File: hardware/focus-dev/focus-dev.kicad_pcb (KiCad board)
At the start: 2 copper layers, 100 x 90 mm, 133 parts, among them J1 USB_C_Receptacle_USB2.0_14P, J2 Conn_01x09, J3 IDC-10, J4 Conn_01x03, J5 Conn_01x01, J6 Conn_01x01, J7 Conn_01x01, J8 IDC-16, J9 XT60, Q1 IPD90N04S4L04, Q2 IPD90N04S4L04, Q3 IPD90N04S4L04, Q4 IPD90N04S4L04, Q5 IPD90N04S4L04, Q6 IPD90N04S4L04, SW1 SW_MEC_5G, SW2 SW_MEC_5G, U1 USBLC6-2SC6, U10 AS5040, U11 LV14340, U2 STM32H523RET6, U3 INA181A3, U4 LM2105D, U5 INA181A3, U6 LM2105D, U7 INA181A3, U8 LM2105D, U9 AS5600, Y1 8MHz

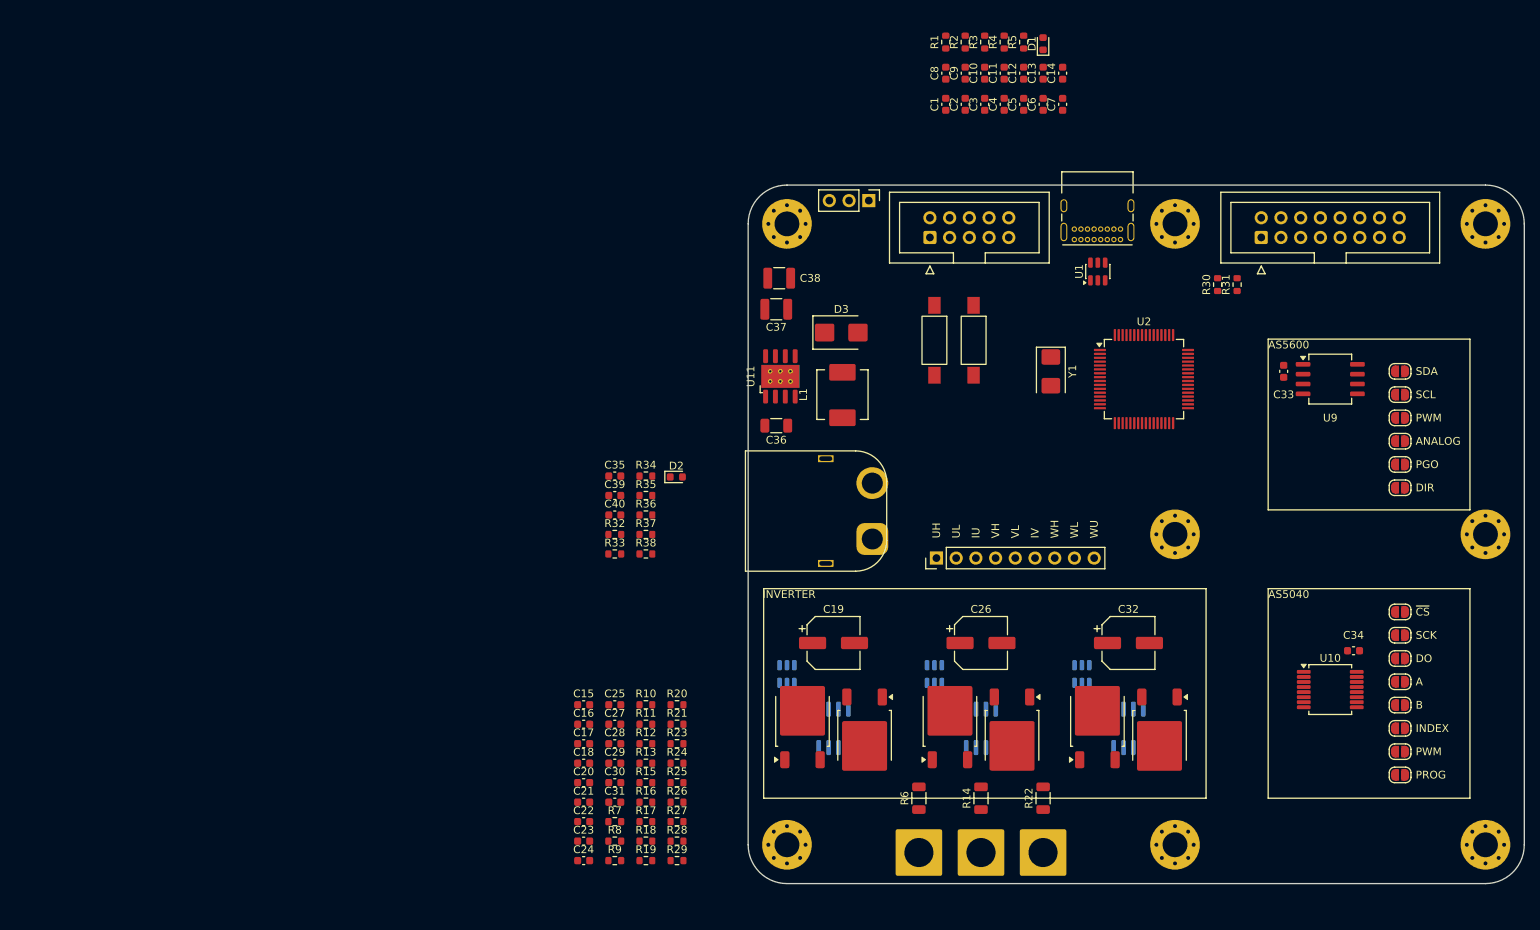
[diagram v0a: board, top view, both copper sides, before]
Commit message: wip: remove onboard encoders
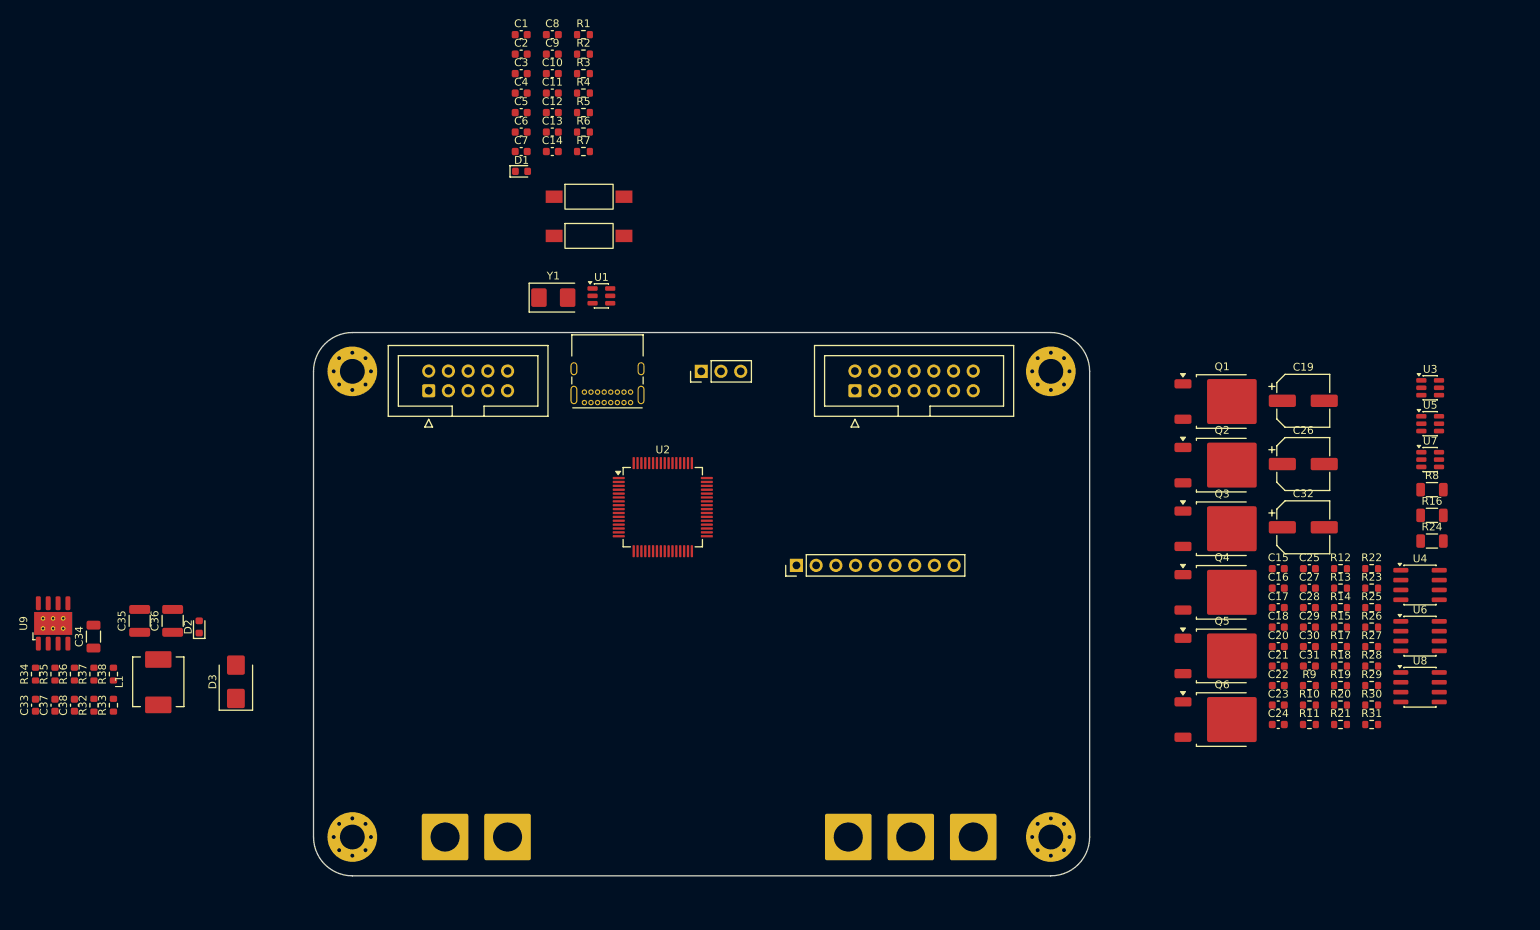
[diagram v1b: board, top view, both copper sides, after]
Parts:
- removed C39: 100n, Capacitor_SMD:C_0603_1608Metric
- removed C40: 22n, Capacitor_SMD:C_0603_1608Metric
- removed H10, H5, H6, H7, H8, H9: MountingHole_Pad, MountingHole:MountingHole_3.2mm_M3_Pad_Via
- removed JP1, JP10, JP11, JP12, JP13, JP14, JP2, JP3, JP4, JP5, JP6, JP7, JP8, JP9: Jumper_2_Open, Jumper:SolderJumper-2_P1.3mm_Open_RoundedPad1.0x1.5mm
- removed U10: AS5040, Package_SO:SSOP-16_5.3x6.2mm_P0.65mm
- removed U11: LV14340, lib:LV14340
- added H3: MountingHole_Pad, MountingHole:MountingHole_3.2mm_M3_Pad_Via, F.Cu at (190.0, 135.0)
- added H4: MountingHole_Pad, MountingHole:MountingHole_3.2mm_M3_Pad_Via, F.Cu at (100.0, 135.0)
- added J10: Conn_01x01, Connector_Wire:SolderWire-4sqmm_1x01_D3mm_OD6mm, F.Cu at (120.0, 135.0)
- C10: value 100n -> 22p
- C12: value 22p -> 100n
- C33: value 100n -> 100n/50V
- C34: value 100n -> 10u/50V; footprint Capacitor_SMD:C_0603_1608Metric -> Capacitor_SMD:C_1206_3216Metric
- C35: value 100n/50V -> 47u/16V; footprint Capacitor_SMD:C_0603_1608Metric -> Capacitor_SMD:C_1210_3225Metric
- C36: value 10u/50V -> 47u/16V; footprint Capacitor_SMD:C_1206_3216Metric -> Capacitor_SMD:C_1210_3225Metric
- C37: value 47u/16V -> 100n; footprint Capacitor_SMD:C_1210_3225Metric -> Capacitor_SMD:C_0603_1608Metric
- C38: value 47u/16V -> 22n; footprint Capacitor_SMD:C_1210_3225Metric -> Capacitor_SMD:C_0603_1608Metric
- C7: value 1u -> 100n
- C8: value 100n -> 1u
- J1: value USB_C_Receptacle_USB2.0_14P -> IDC-10; footprint Connector_USB:USB_C_Receptacle_GCT_USB4085 -> Connector_IDC:IDC-Header_2x05_P2.54mm_Vertical
- J2: value Conn_01x09 -> USB_C_Receptacle_USB2.0_14P; footprint Connector_PinHeader_2.54mm:PinHeader_1x09_P2.54mm_Vertical -> Connector_USB:USB_C_Receptacle_GCT_USB4085
- J3: value IDC-10 -> IDC-14; footprint Connector_IDC:IDC-Header_2x05_P2.54mm_Vertical -> Connector_IDC:IDC-Header_2x07_P2.54mm_Vertical
- J4: value Conn_01x03 -> Conn_01x09; footprint Connector_PinHeader_2.54mm:PinHeader_1x03_P2.54mm_Vertical -> Connector_PinHeader_2.54mm:PinHeader_1x09_P2.54mm_Vertical
- J5: value Conn_01x01 -> Conn_01x03; footprint Connector_Wire:SolderWire-4sqmm_1x01_D3mm_OD6mm -> Connector_PinHeader_2.54mm:PinHeader_1x03_P2.54mm_Vertical
- J8: value IDC-16 -> Conn_01x01; footprint Connector_IDC:IDC-Header_2x08_P2.54mm_Vertical -> Connector_Wire:SolderWire-4sqmm_1x01_D3mm_OD6mm
- J9: value XT60 -> Conn_01x01; footprint lib:XT60PW-M -> Connector_Wire:SolderWire-4sqmm_1x01_D3mm_OD6mm
- R10, R19: value 4.7k -> 68
- R11: value 4.7k -> 47k
- R12, R26: value 68 -> 4.7k
- R13, R18, R21, R27: value 47k -> 4.7k
- R14, R22: value 2m -> 68; footprint Resistor_SMD:R_1206_3216Metric -> Resistor_SMD:R_0603_1608Metric
- R15, R23: value 10 -> 47k
- R16, R24: value 4.7k -> 2m; footprint Resistor_SMD:R_0603_1608Metric -> Resistor_SMD:R_1206_3216Metric
- R17: value 68 -> 10
- R20: value 68 -> 47k
- R25: value 4.7k -> 10
- R3, R4: value 10k -> 4.7k
- R30: value 10k -> 68
- R31: value 10k -> 47k
- R5: value 1k -> 4.7k
- R6: value 2m -> 10k; footprint Resistor_SMD:R_1206_3216Metric -> Resistor_SMD:R_0603_1608Metric
- R7: value 10 -> 1k
- R8: value 68 -> 2m; footprint Resistor_SMD:R_0603_1608Metric -> Resistor_SMD:R_1206_3216Metric
- R9: value 47k -> 10
- SW1, SW2: value SW_MEC_5G -> SW_Push
- U3, U4, U5, U6, U7, U8: moved to F.Cu
- U9: value AS5600 -> LV14340; footprint Package_SO:SOIC-8_5.3x6.2mm_P1.27mm -> lib:LV14340
- moved U9 167.5 mm to (61.5, 107.5), turned to 90 degrees
- moved C33 166.5 mm to (59.2, 118.0), turned to 90 degrees
- moved C34 162.4 mm to (66.7, 109.2), turned to 90 degrees
- moved R8 114.6 mm to (239.1, 90.2)
- moved R16 107.8 mm to (239.1, 93.6)
- moved C38 106.2 mm to (64.2, 118.0), turned to 90 degrees
- moved C37 106.0 mm to (61.7, 118.0), turned to 90 degrees
- moved R24 101.4 mm to (239.1, 96.9)
- moved R6 96.1 mm to (129.8, 44.2), turned to 0 degrees
- moved L1 95.6 mm to (75.0, 115.0)
- moved R12 92.3 mm to (227.3, 100.4)
- moved R13 92.3 mm to (227.3, 102.9)
- moved R17 92.3 mm to (227.3, 110.5)
- moved R18 92.3 mm to (227.3, 113.0)
- moved R19 92.3 mm to (227.3, 115.5)
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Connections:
- C10 pad 1: /control/STM_USER_BUTTON -> /control/STM_OSC_IN
- C11 pad 1: /control/STM_OSC_IN -> /control/STM_OSC_OUT
- C12 pad 1: /control/STM_OSC_OUT -> /control/STM_USER_BUTTON
- C33 pad 1: +3.3V -> Net-(U9-BOOT)
- C33 pad 2: GND -> Net-(D3-K)
- C34 pad 1: +3.3V -> VBUS
- C35 pad 1: Net-(U11-BOOT) -> +3.3V
- C35 pad 2: Net-(D3-K) -> GND
- C36 pad 1: VBUS -> +3.3V
- C37 pad 1: +3.3V -> POWER_SENSE
- C38 pad 1: +3.3V -> GND
- C38 pad 2: GND -> Net-(U9-SS)
- J3 pad 1: /control/STM_RESET -> +3.3V
- J3 pad 10: unconnected-(J3-Pin_10-Pad10) -> /control/ENCODER_SPI_CS
- J3 pad 2: /control/STM_SWCLK -> unconnected-(J3-Pin_2-Pad2)
- J3 pad 3: unconnected-(J3-Pin_3-Pad3) -> +3.3V
- J3 pad 4: /control/STM_SWDIO -> /control/ENCODER_SPI_MISO
- J3 pad 5: GND -> /control/ENCODER_A
- J3 pad 6: GND -> /control/ENCODER_SPI_MOSI
- J3 pad 7: +3.3V -> /control/ENCODER_B
- J3 pad 8: +3.3V -> /control/ENCODER_SPI_SCK
- J3 pad 9: unconnected-(J3-Pin_9-Pad9) -> /control/ENCODER_INDEX
- J4 pad 1: GND -> MOTOR_PWM_UH
- J4 pad 2: /control/STM_USER_GPIO2 -> MOTOR_PWM_UL
- J4 pad 3: /control/STM_USER_GPIO1 -> MOTOR_SENSE_U
- J5 pad 1: Net-(J5-Pin_1) -> GND
- J8 pad 1: +3.3V -> Net-(J8-Pin_1)
- J9 pad 1: GND -> VBUS
- R10 pad 1: Net-(U3-REF) -> Net-(U4-GH)
- R10 pad 2: +3.3V -> Net-(Q1-G)
- R11 pad 1: Net-(U3-REF) -> Net-(Q1-G)
- R11 pad 2: GND -> /inverter/PHASE_U
- R12 pad 1: Net-(U4-GL) -> Net-(U3-REF)
- R12 pad 2: Net-(Q2-G) -> +3.3V
- R13 pad 1: Net-(Q2-G) -> Net-(U3-REF)
- R14 pad 1: /inverter/PHASE_V -> Net-(U4-GL)
- R14 pad 2: Net-(J6-Pin_1) -> Net-(Q2-G)
- R15 pad 1: Net-(R15-Pad1) -> Net-(Q2-G)
- R15 pad 2: MOTOR_SENSE_V -> GND
- R16 pad 1: Net-(U5-REF) -> /inverter/PHASE_V
- R16 pad 2: +3.3V -> Net-(J7-Pin_1)
- R17 pad 1: Net-(U6-GH) -> Net-(R17-Pad1)
- R17 pad 2: Net-(Q3-G) -> MOTOR_SENSE_V
- R18 pad 1: Net-(Q3-G) -> Net-(U5-REF)
- R18 pad 2: /inverter/PHASE_V -> +3.3V
- R19 pad 1: Net-(U5-REF) -> Net-(U6-GH)
- R19 pad 2: GND -> Net-(Q3-G)
- R20 pad 1: Net-(U6-GL) -> Net-(Q3-G)
- R20 pad 2: Net-(Q4-G) -> /inverter/PHASE_V
- R21 pad 1: Net-(Q4-G) -> Net-(U5-REF)
- R22 pad 1: /inverter/PHASE_W -> Net-(U6-GL)
- R22 pad 2: Net-(J7-Pin_1) -> Net-(Q4-G)
- R23 pad 1: Net-(R23-Pad1) -> Net-(Q4-G)
- R23 pad 2: MOTOR_SENSE_W -> GND
- R24 pad 1: Net-(U7-REF) -> /inverter/PHASE_W
- R24 pad 2: +3.3V -> Net-(J8-Pin_1)
- R25 pad 1: Net-(U7-REF) -> Net-(R25-Pad1)
- R25 pad 2: GND -> MOTOR_SENSE_W
- R26 pad 1: Net-(U8-GH) -> Net-(U7-REF)
- R26 pad 2: Net-(Q5-G) -> +3.3V
- R27 pad 1: Net-(Q5-G) -> Net-(U7-REF)
- R27 pad 2: /inverter/PHASE_W -> GND
- R28 pad 1: Net-(U8-GL) -> Net-(U8-GH)
- R28 pad 2: Net-(Q6-G) -> Net-(Q5-G)
- R29 pad 1: Net-(Q6-G) -> Net-(Q5-G)
- R29 pad 2: GND -> /inverter/PHASE_W
- R30 pad 1: +3.3V -> Net-(U8-GL)
- R30 pad 2: ENCODER_I2C_SCL -> Net-(Q6-G)
- R31 pad 1: +3.3V -> Net-(Q6-G)
- R31 pad 2: ENCODER_I2C_SDA -> GND
- R35 pad 2: Net-(U11-FB) -> Net-(U9-FB)
- R37 pad 1: Net-(U11-RT/SYNC) -> Net-(U9-RT/SYNC)
- R38 pad 1: Net-(U11-FB) -> Net-(U9-FB)
- R4 pad 2: /control/STM_USER_BUTTON -> /control/ENCODER_I2C_SCL
- R5 pad 1: /control/STM_USER_LED -> +3.3V
- R5 pad 2: Net-(D1-A) -> /control/ENCODER_I2C_SDA
- R6 pad 1: /inverter/PHASE_U -> +3.3V
- R6 pad 2: Net-(J5-Pin_1) -> /control/STM_USER_BUTTON
- R7 pad 1: Net-(R7-Pad1) -> /control/STM_USER_LED
- R7 pad 2: MOTOR_SENSE_U -> Net-(D1-A)
- R8 pad 1: Net-(U4-GH) -> /inverter/PHASE_U
- R8 pad 2: Net-(Q1-G) -> Net-(J6-Pin_1)
- R9 pad 1: Net-(Q1-G) -> Net-(R9-Pad1)
- R9 pad 2: /inverter/PHASE_U -> MOTOR_SENSE_U
- SW1 pad 2: GND -> /control/STM_RESET
- SW2 pad 2: GND -> /control/STM_USER_BUTTON
- U2 pad 11: ENCODER_ANALOG -> POWER_SENSE
- U2 pad 14: ENCODER_A -> /control/ENCODER_A
- U2 pad 15: ENCODER_B -> /control/ENCODER_B
- U2 pad 20: ENCODER_SPI_CS -> /control/ENCODER_SPI_CS
- U2 pad 21: ENCODER_SPI_SCK -> /control/ENCODER_SPI_SCK
- U2 pad 22: ENCODER_SPI_MISO -> /control/ENCODER_SPI_MISO
- U2 pad 23: ENCODER_SPI_MOSI -> /control/ENCODER_SPI_MOSI
- U2 pad 24: POWER_SENSE -> unconnected-(U2-PC4-Pad24)
- U2 pad 50: ENCODER_INDEX -> /control/ENCODER_INDEX
- U2 pad 51: ENCODER_CTRL1 -> unconnected-(U2-PC10-Pad51)
- U2 pad 52: ENCODER_CTRL2 -> unconnected-(U2-PC11-Pad52)
- U2 pad 53: ENCODER_PWM -> unconnected-(U2-PC12-Pad53)
- U2 pad 58: ENCODER_I2C_SCL -> /control/ENCODER_I2C_SCL
- U2 pad 59: ENCODER_I2C_SDA -> /control/ENCODER_I2C_SDA
- U3 pad 1: Net-(R7-Pad1) -> Net-(R9-Pad1)
- U3 pad 4: Net-(J5-Pin_1) -> Net-(J6-Pin_1)
- U5 pad 1: Net-(R15-Pad1) -> Net-(R17-Pad1)
- U5 pad 4: Net-(J6-Pin_1) -> Net-(J7-Pin_1)
- U7 pad 1: Net-(R23-Pad1) -> Net-(R25-Pad1)
- U7 pad 4: Net-(J7-Pin_1) -> Net-(J8-Pin_1)
- U9 pad 1: +3.3V -> Net-(U9-BOOT)
- U9 pad 2: +3.3V -> VBUS
- U9 pad 3: Net-(JP5-A) -> unconnected-(U9-EN-Pad3)
- U9 pad 4: GND -> Net-(U9-RT/SYNC)
- U9 pad 5: Net-(JP2-B) -> Net-(U9-FB)
- U9 pad 6: Net-(JP1-A) -> Net-(U9-SS)
- U9 pad 7: Net-(JP3-A) -> GND
- U9 pad 8: Net-(JP4-B) -> Net-(D3-K)
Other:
- board size 100 x 90 mm -> 100 x 70 mm
- board text removed: "A"
- board text removed: "ANALOG"
- board text removed: "AS5040"
- board text removed: "AS5600"
- board text removed: "B"
- board text removed: "DIR"
- board text removed: "DO"
- board text removed: "INDEX"
- board text removed: "INVERTER"
- board text removed: "IU"
- board text removed: "IV"
- board text removed: "PGO"
- board text removed: "PROG"
- board text removed: "PWM"
- board text removed: "SCK"
- board text removed: "SCL"
- board text removed: "SDA"
- board text removed: "UH"
- board text removed: "UL"
- board text removed: "VH"
- board text removed: "VL"
- board text removed: "WH"
- board text removed: "WL"
- board text removed: "WU"
- board text removed: "~{CS}"

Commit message: wip: layout
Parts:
- C15, C16, C17, C20, C21, C22, C24, C25, C27, C29, C30, C31, R10, R11, R12, R13, R14, R15, R18, R19, R20, R21, R22, R23, R26, R27, R28, R29, R30, R31, U3, U4, U5, U6, U7, U8: moved to B.Cu
- moved C19 91.0 mm to (146.0, 128.0), turned to 180 degrees
- moved C26 82.9 mm to (146.0, 119.0), turned to 180 degrees
- moved U4 78.8 mm to (163.0, 128.0)
- moved C32 78.0 mm to (146.0, 110.0), turned to 180 degrees
- moved U6 75.2 mm to (163.0, 119.0)
- moved U3 75.1 mm to (181.5, 125.5), turned to 180 degrees
- moved U8 74.8 mm to (163.0, 110.0)
- moved Q1 73.0 mm to (158.0, 128.0), turned to 180 degrees
- moved R29 70.4 mm to (161.0, 114.0)
- moved R8 67.9 mm to (182.0, 127.0), turned to 180 degrees
- moved C16 67.9 mm to (157.5, 131.0), turned to 90 degrees
- moved U5 67.6 mm to (181.5, 117.5), turned to 180 degrees
- moved R20 66.5 mm to (161.0, 123.0)
- moved R25 66.4 mm to (165.8, 94.5)
- moved R28 66.3 mm to (165.0, 114.0)
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
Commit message: wip: rest of the layout
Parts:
- moved C37 25.8 mm to (127.6, 123.5)
- moved R34 25.8 mm to (125.6, 123.5)
- moved R12 12.5 mm to (184.0, 132.0), turned to -90 degrees
- moved R18 12.5 mm to (184.0, 124.0), turned to -90 degrees
- moved R26 12.5 mm to (184.0, 116.0), turned to -90 degrees
- moved R4 10.8 mm to (178.0, 93.8)
- moved R13 10.6 mm to (182.0, 132.0), turned to -90 degrees
- moved R21 10.6 mm to (182.0, 124.0), turned to -90 degrees
- moved R27 10.6 mm to (182.0, 116.0), turned to -90 degrees
- moved C15 10.3 mm to (179.0, 132.0), turned to -90 degrees
- moved C21 10.3 mm to (179.0, 124.0), turned to -90 degrees
- moved C27 10.3 mm to (179.0, 116.0), turned to -90 degrees
- moved J10 10.3 mm to (109.8, 134.8)
- moved R10 9.60 mm to (155.4, 132.0)
- moved R19 9.60 mm to (155.4, 123.0)
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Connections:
- J3 pad 4: /control/ENCODER_SPI_MISO -> /control/ENCODER_SPI_MOSI
- J3 pad 6: /control/ENCODER_SPI_MOSI -> /control/ENCODER_SPI_MISO
- J4 pad 3: MOTOR_SENSE_U -> MOTOR_PWM_VH
- J4 pad 4: MOTOR_PWM_VH -> MOTOR_PWM_VL
- J4 pad 5: MOTOR_PWM_VL -> MOTOR_PWM_WH
- J4 pad 6: MOTOR_SENSE_V -> MOTOR_PWM_WL
- J4 pad 7: MOTOR_PWM_WH -> MOTOR_SENSE_U
- J4 pad 8: MOTOR_PWM_WL -> MOTOR_SENSE_V
- U2 pad 2: unconnected-(U2-PC13-Pad2) -> /control/STM_USER_BUTTON
- U2 pad 26: /control/STM_USER_BUTTON -> unconnected-(U2-PB0-Pad26)
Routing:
- net GND: track 0.00 -> 114.2 mm, vias 0 -> 139
- net /control/ENCODER_SPI_CS: track 0.00 -> 85.4 mm, vias 0 -> 1
- net /control/ENCODER_SPI_SCK: track 0.00 -> 81.7 mm, vias 0 -> 1
- net MOTOR_SENSE_W: track 0.00 -> 79.3 mm, vias 0 -> 2
- net /control/ENCODER_SPI_MISO: track 0.00 -> 78.6 mm, vias 0 -> 1
- net MOTOR_SENSE_U: track 0.00 -> 77.4 mm, vias 0 -> 2
- net +3.3V: track 0.00 -> 77.1 mm, vias 0 -> 29
- net MOTOR_SENSE_V: track 0.00 -> 76.9 mm, vias 0 -> 2
- net /control/ENCODER_SPI_MOSI: track 0.00 -> 74.2 mm, vias 0 -> 1
- net /control/STM_RESET: track 0.00 -> 72.4 mm, vias 0 -> 2
- net /control/ENCODER_B: track 0.00 -> 70.0 mm, vias 0 -> 1
- net /control/ENCODER_A: track 0.00 -> 67.9 mm, vias 0 -> 1
- net /control/ENCODER_I2C_SCL: track 0.00 -> 64.8 mm, vias 0 -> 2
- net /control/ENCODER_I2C_SDA: track 0.00 -> 63.6 mm, vias 0 -> 2
- net /control/ENCODER_INDEX: track 0.00 -> 58.0 mm, vias 0 -> 1
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- added copper zone on F.Cu, net +3.3V
- added copper zone on In1.Cu, net +3.3V
- added copper zone on F.Cu, net /inverter/PHASE_U
- added copper zone on F.Cu, net /inverter/PHASE_V
- added copper zone on F.Cu, net /inverter/PHASE_W
- added copper zone on B.Cu, net GND
- added copper zone on F.Cu, net GND
- added copper zone on In2.Cu, net GND
- added copper zone on F.Cu, net Net-(D3-K)
- added copper zone on F.Cu, net VBUS
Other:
- copper layers 2 -> 4
- board text added: "3.3V"
- board text added: "A"
- board text added: "B"
- board text added: "BLDC motor driver FOCUS V1.0 by Eryk Możdżeń February 2026"
- board text added: "CS"
- board text added: "ENCODER"
- board text added: "GND"
- board text added: "INDEX"
- board text added: "JLCJLCJLCJLC"
- board text added: "MISO"
- board text added: "MOSI"
- board text added: "NC"
- board text added: "PB1"
- board text added: "PB2"
- board text added: "RESET"
- board text added: "SCK"
- board text added: "SCL"
- board text added: "SDA"
- board text added: "SENSE_U"
- board text added: "SENSE_V"
- board text added: "SENSE_W"
- board text added: "SWCLK"
- board text added: "SWD"
- board text added: "SWDIO"
- board text added: "U"
- board text added: "UH"
- board text added: "UL"
- board text added: "USB"
- board text added: "V"
- board text added: "VBUS"
- board text added: "VH"
- board text added: "VL"
- board text added: "W"
- board text added: "WH"
- board text added: "WL"
